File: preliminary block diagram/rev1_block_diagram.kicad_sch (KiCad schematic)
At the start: 16 parts, among them SW1 ???, U29 LMX2594+100MHz oscillator, U30 PA, U31 HMC451, U32 LNA, U33 ADP-2-1W, U34 10dB, U35 Mixer, U37 Mixer, U39 ADP-2-1W

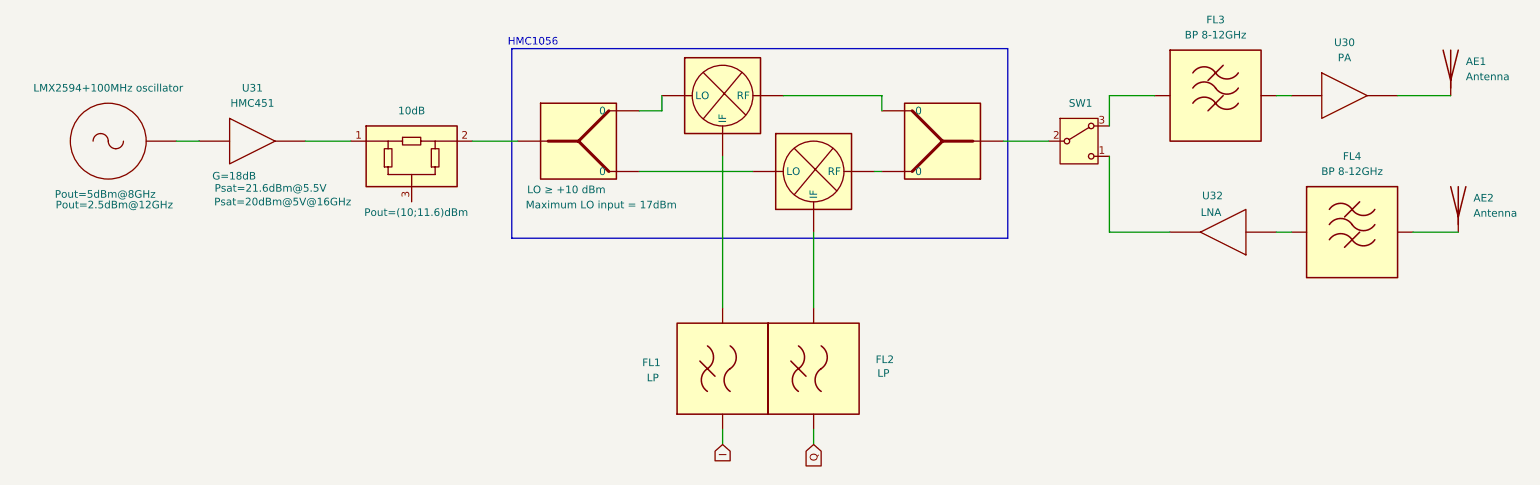
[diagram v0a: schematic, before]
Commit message: Added selected components to the block diagram
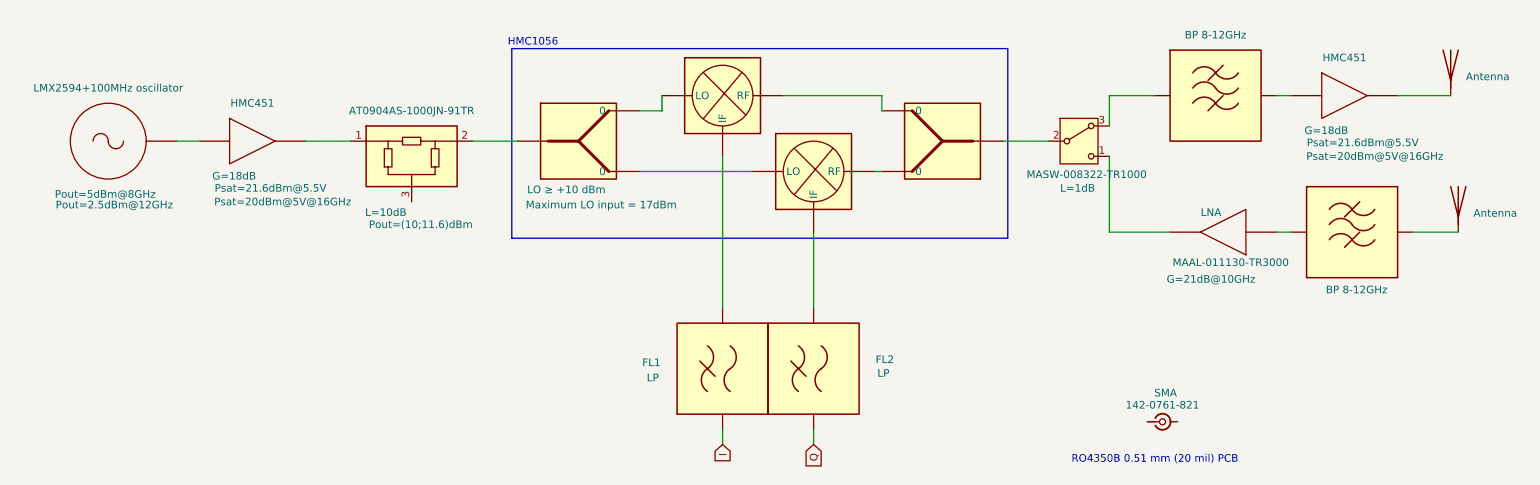
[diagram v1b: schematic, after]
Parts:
- removed U30: PA, symbol custom_rf_symbols:Amplifier
- added J1: 142-0761-821, symbol Connector:Conn_Coaxial_Small
- added U36: HMC451, symbol custom_rf_symbols:Amplifier
- SW1: value ??? -> ~; footprint Button_Switch_SMD:Nidec_Copal_CAS-120A -> (none); Field5 (none) -> L=1dB
- U32: Field5 (none) -> G=21dB@10GHz
- U34: value 10dB -> AT0904AS-1000JN-91TR; footprint RF_Converter:RF_Attenuator_Susumu_PAT1220 -> (none); Field6 (none) -> L=10dB
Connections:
- net at FL3.3 (OUT): now also U36.1 (IN)
- net at AE1.1 (A): now also U36.2 (OUT)
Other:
- note added: "RO4350B 0.51 mm (20 mil) PCB"
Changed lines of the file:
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@@
+		)
+	)
+	(text "RO4350B 0.51 mm (20 mil) PCB\n"
+		(exclude_from_sim no)
+		(at 210.82 143.51 0)
+		(effects
+			(font
+				(size 1.27 1.27)
+			)
 		)
 	)
@@
 					(size 1.27 1.27)
 				)
-			)
-		)
-		(property "Value" "???"
+				(hide yes)
+			)
+		)
+		(property "Value" "~"
 			(at 198.12 83.82 0)
 			(effects
@@
 			)
 		)
-		(property "Footprint" "Button_Switch_SMD:Nidec_Copal_CAS-120A"
+		(property "Footprint" ""
 			(at 198.12 100.33 0)
 			(effects
@@
 			)
 		)
-		(property "Datasheet" "https://www.nidec-components.com/e/catalog/switch/cas.pdf"
+		(property "Datasheet" "https://cz.mouser.com/datasheet/3/829/1/MASW-008322.pdf"
 			(at 198.12 97.79 0)
 			(effects
@@
 			)
 		)
-		(property "Description" "Switch, single pole double throw"
-			(at 198.12 90.17 0)
-			(effects
-				(font
-					(size 1.27 1.27)
-				)
-				(hide yes)
+		(property "Description" "MASW-008322-TR1000"
+			(at 199.39 95.758 0)
+			(effects
+				(font
+					(size 1.27 1.27)
+				)
+			)
+		)
+		(property "Field5" "L=1dB"
+			(at 197.866 98.044 0)
+			(effects
+				(font
+					(size 1.27 1.27)
+				)
 			)
 		)
@@
 				)
 				(justify left)
+				(hide yes)
 			)
 		)
@@
 					(size 1.27 1.27)
 				)
+				(hide yes)
 			)
 		)
@@
 			)
 		)
-		(property "Datasheet" ""
+		(property "Datasheet" "https://cz.mouser.com/en/ProductDetail/MACOM/MAAL-011130-TR3000?qs=byeeYqUIh0Mgo6fB7YXTZg%3D%3D"
 			(at 223.52 110.49 0)
 			(effects
@@
 			)
 		)
-		(property "Description" ""
+		(property "Description" "MAAL-011130-TR3000"
 			(at 223.52 110.49 0)
 			(effects
@@
 					(size 1.27 1.27)
 				)
-				(hide yes)
+			)
+		)
+		(property "Field5" "G=21dB@10GHz"
+			(at 220.218 113.284 0)
+			(effects
+				(font
+					(size 1.27 1.27)
+				)
 			)
 		)
@@
 					(size 1.27 1.27)
 				)
+				(hide yes)
 			)
 		)
@@
 				(path "/0b61a76d-2d09-44e4-b8e3-89709cafea27/32a8c150-5b91-45e6-a88c-e22f86ba438b"
 					(reference "FL3")
+					(unit 1)
+				)
+			)
+		)
+	)
+	(symbol
+		(lib_id "custom_rf_symbols:Amplifier")
+		(at 241.3 77.47 0)
+		(unit 1)
+		(exclude_from_sim no)
+		(in_bom yes)
+		(on_board yes)
+		(dnp no)
+		(property "Reference" "U36"
+			(at 242.57 73.66 0)
+			(effects
+				(font
+					(size 1.27 1.27)
+				)
+				(hide yes)
+			)
+		)
+		(property "Value" "HMC451"
+			(at 242.57 76.2 0)
+			(effects
+				(font
+					(size 1.27 1.27)
+				)
+			)
+		)
+		(property "Footprint" ""
+			(at 241.3 77.47 0)
+			(effects
+				(font
+					(size 1.27 1.27)
+				)
+				(hide yes)
+			)
+		)
+		(property "Datasheet" ""
+			(at 241.3 77.47 0)
+			(effects
+				(font
+					(size 1.27 1.27)
+				)
+				(hide yes)
+			)
+		)
+		(property "Description" "G=18dB"
+			(at 239.522 88.392 0)
+			(effects
+				(font
+					(size 1.27 1.27)
+				)
+			)
+		)
+		(property "Field5" "Psat=21.6dBm@5.5V"
+			(at 245.618 90.424 0)
+			(effects
+				(font
+					(size 1.27 1.27)
+				)
+			)
+		)
+		(property "Field6" "Psat=20dBm@5V@16GHz"
+			(at 247.65 92.71 0)
+			(effects
+				(font
+					(size 1.27 1.27)
+				)
+			)
+		)
+		(pin "2"
+		)
+		(pin "1"
+		)
+		(instances
+			(project "preliminary block diagram"
+				(path "/0b61a76d-2d09-44e4-b8e3-89709cafea27/32a8c150-5b91-45e6-a88c-e22f86ba438b"
+					(reference "U36")
 					(unit 1)
 				)
@@
 				)
 				(justify left)
+				(hide yes)
 			)
 		)
@@
 	)
 	(symbol
-		(lib_id "custom_rf_symbols:Amplifier")
-		(at 241.3 77.47 0)
-		(unit 1)
-		(exclude_from_sim no)
-		(in_bom yes)
-		(on_board yes)
-		(dnp no)
-		(fields_autoplaced yes)
-		(property "Reference" "U30"
-			(at 242.57 73.66 0)
-			(effects
-				(font
-					(size 1.27 1.27)
-				)
-			)
-		)
-		(property "Value" "PA"
-			(at 242.57 76.2 0)
-			(effects
-				(font
-					(size 1.27 1.27)
-				)
-			)
-		)
-		(property "Footprint" ""
-			(at 241.3 77.47 0)
-			(effects
-				(font
-					(size 1.27 1.27)
-				)
-				(hide yes)
-			)
-		)
-		(property "Datasheet" ""
-			(at 241.3 77.47 0)
-			(effects
-				(font
-					(size 1.27 1.27)
-				)
-				(hide yes)
-			)
-		)
-		(property "Description" ""
-			(at 241.3 77.47 0)
-			(effects
-				(font
-					(size 1.27 1.27)
-				)
-				(hide yes)
-			)
-		)
-		(pin "2"
-		)
-		(pin "1"
-		)
-		(instances
-			(project "preliminary block diagram"
-				(path "/0b61a76d-2d09-44e4-b8e3-89709cafea27/32a8c150-5b91-45e6-a88c-e22f86ba438b"
-					(reference "U30")
-					(unit 1)
-				)
-			)
-		)
-	)
-	(symbol
 		(lib_id "custom_rf_symbols:Oscillator")
 		(at 39.37 87.63 0)
@@
 			)
 		)
-		(property "Value" "10dB"
+		(property "Value" "AT0904AS-1000JN-91TR"
 			(at 86.36 85.09 0)
 			(effects
@@
 			)
 		)
-		(property "Footprint" "RF_Converter:RF_Attenuator_Susumu_PAT1220"
+		(property "Footprint" ""
 			(at 86.36 92.71 0)
 			(effects
@@
 			)
 		)
-		(property "Datasheet" "https://www.susumu.co.jp/common/pdf/n_catalog_partition16_en.pdf"
+		(property "Datasheet" "https://cz.mouser.com/en/ProductDetail/Vishay-Barry-Industries/AT0904AS-1000JN-91TR?qs=ulEaXIWI0c9CMXIQQzzR1g%3D%3D"
 			(at 80.01 86.36 0)
 			(effects
@@
 		)
 		(property "Description" "Pout=(10;11.6)dBm"
-			(at 87.122 102.108 0)
+			(at 87.884 104.14 0)
+			(effects
+				(font
+					(size 1.27 1.27)
+				)
+			)
+		)
+		(property "Field5" ""
+			(at 86.36 92.71 0)
+			(effects
+				(font
+					(size 1.27 1.27)
+				)
+				(hide yes)
+			)
+		)
+		(property "Field6" "L=10dB"
+			(at 82.042 102.108 0)
 			(effects
 				(font
@@
 					(size 1.27 1.27)
 				)
+				(hide yes)
 			)
 		)
@@
 				(path "/0b61a76d-2d09-44e4-b8e3-89709cafea27/32a8c150-5b91-45e6-a88c-e22f86ba438b"
 					(reference "FL1")
+					(unit 1)
+				)
+			)
+		)
+	)
+	(symbol
+		(lib_id "Connector:Conn_Coaxial_Small")
+		(at 212.09 137.16 0)
+		(unit 1)
+		(exclude_from_sim no)
+		(in_bom yes)
+		(on_board yes)
+		(dnp no)
+		(property "Reference" "J1"
+			(at 211.5704 130.81 0)
+			(effects
+				(font
+					(size 1.27 1.27)
+				)
+				(hide yes)
+			)
+		)
+		(property "Value" "142-0761-821"
+			(at 212.09 134.366 0)
+			(effects
+				(font
+					(size 1.27 1.27)
+				)
+			)
+		)
+		(property "Footprint" ""
+			(at 212.09 137.16 0)
+			(effects
+				(font
+					(size 1.27 1.27)
+				)
+				(hide yes)
+			)
+		)
+		(property "Datasheet" "https://cz.mouser.com/en/ProductDetail/Johnson-Cinch-Connectivity-Solutions/142-0761-821?qs=KmQR6Yc%252BszUNTpdqd2n2zQ%3D%3D"
+			(at 212.09 137.16 0)
+			(effects
+				(font
+					(size 1.27 1.27)
+				)
+				(hide yes)
+			)
+		)
+		(property "Description" "SMA"
+			(at 212.6096 132.334 0)
+			(effects
+				(font
+					(size 1.27 1.27)
+				)
+			)
+		)
+		(pin "2"
+		)
+		(pin "1"
+		)
+		(instances
+			(project "preliminary block diagram"
+				(path "/0b61a76d-2d09-44e4-b8e3-89709cafea27/32a8c150-5b91-45e6-a88c-e22f86ba438b"
+					(reference "J1")
 					(unit 1)
 				)
@@
 		(on_board yes)
 		(dnp no)
-		(fields_autoplaced yes)
 		(property "Reference" "FL4"
 			(at 243.84 92.71 0)
@@
 					(size 1.27 1.27)
 				)
+				(hide yes)
 			)
 		)
 		(property "Value" "BP 8-12GHz"
-			(at 243.84 95.25 0)
-			(effects
-				(font
+			(at 244.602 115.062 0)
+			(effects
+				(font
